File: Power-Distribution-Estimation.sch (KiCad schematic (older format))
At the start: 0 parts

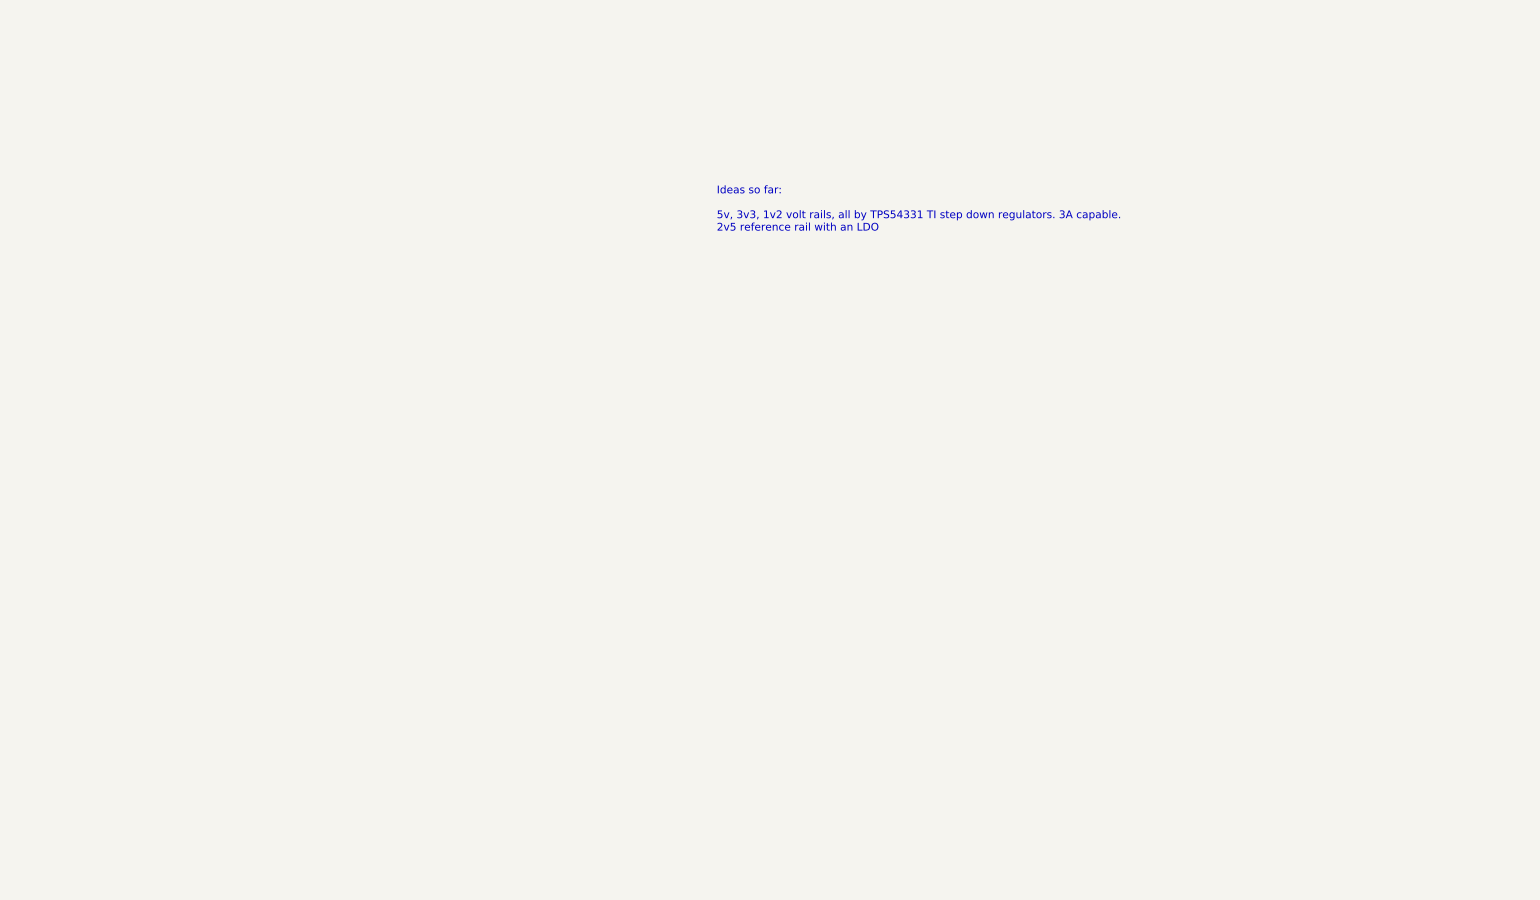
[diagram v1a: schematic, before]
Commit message: Continued work on schematic and board planning
Signed-off-by: Eldalote <Eldalote.Electronics@gmail.com>
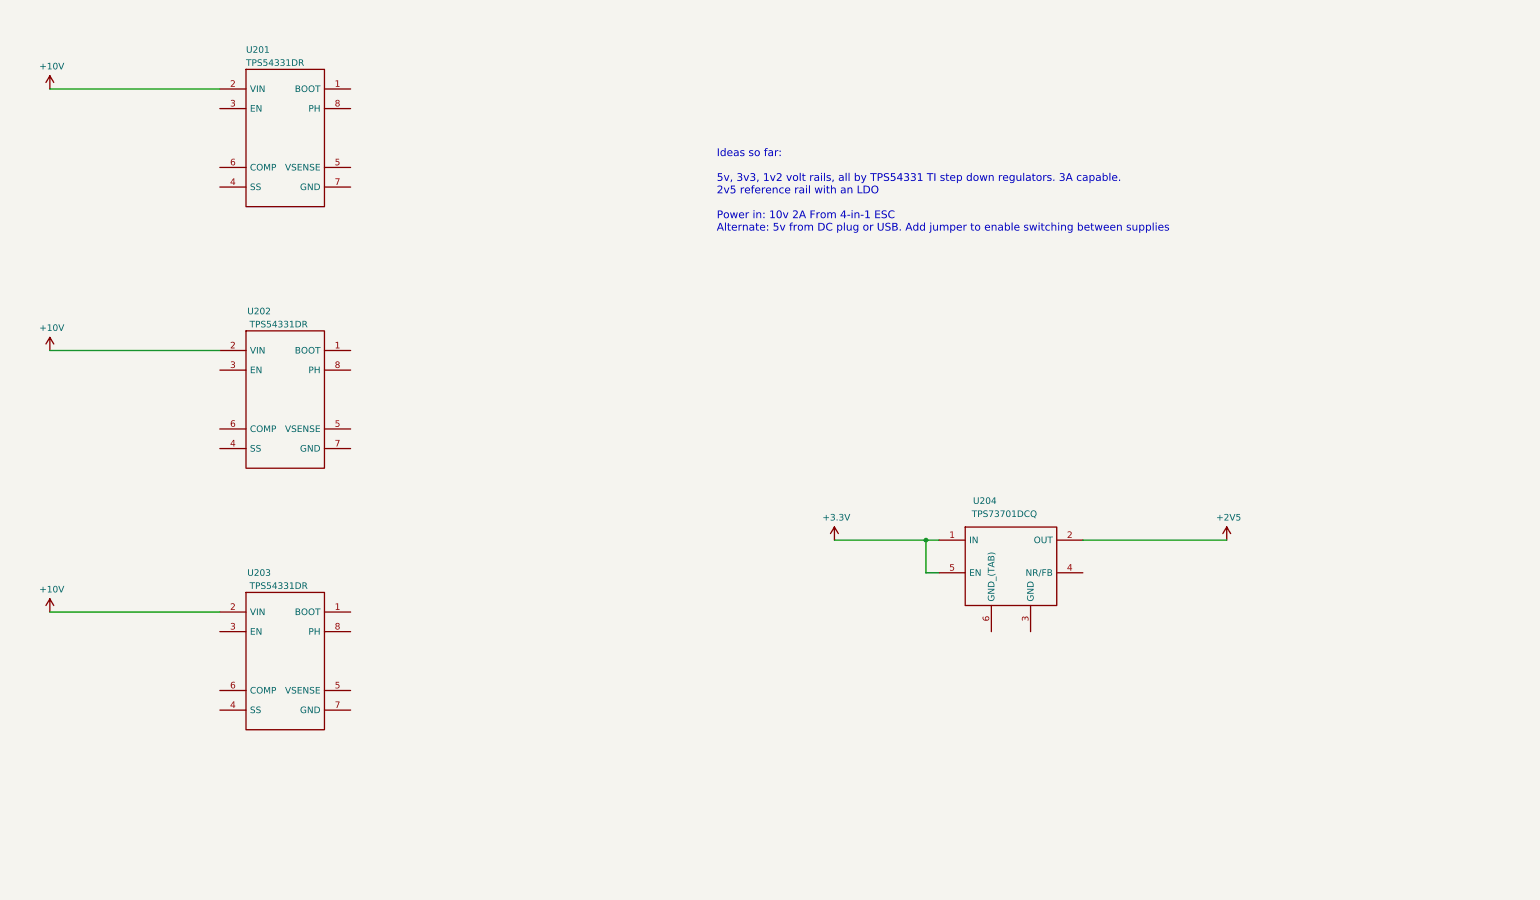
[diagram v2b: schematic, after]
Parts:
- added U201, U202, U203: TPS54331DR, SOIC127P600X175-8N, symbol SamacSys_Parts:TPS54331DR
- added U204: TPS73701DCQ, SOT127P706X180-6N, symbol SamacSys_Parts:TPS73701DCQ
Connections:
- new net +10V: U201.2 (VIN), U202.2 (VIN), U203.2 (VIN)
- new net +2V5: U204.2 (OUT)
- new net +3V3: U204.1 (IN), U204.5 (EN)
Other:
- note added: "Ideas so far:\n\n5v, 3v3, 1v2 volt rails, all by TPS54331 TI step down regulators. 3A capable.\n2v5 reference rail with an LDO\n\nPower in: 10v 2A From 4-in-1 ESC\nAlternate: 5v from DC plug or USB. Add jumper to enable switching between supplies"
- note removed: "Ideas so far:\n\n5v, 3v3, 1v2 volt rails, all by TPS54331 TI step down regulators. 3A capable.\n2v5 reference rail with an LDO"
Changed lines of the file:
@@
 $EndDescr
 Text Notes 6100 2250 0    59   ~ 0
-Ideas so far:\n\n5v, 3v3, 1v2 volt rails, all by TPS54331 TI step down regulators. 3A capable.\n2v5 reference rail with an LDO
+Ideas so far:\n\n5v, 3v3, 1v2 volt rails, all by TPS54331 TI step down regulators. 3A capable.\n2v5 reference rail with an LDO\n\nPower in: 10v 2A From 4-in-1 ESC\nAlternate: 5v from DC plug or USB. Add jumper to enable switching between supplies
+$Comp
+L SamacSys_Parts:TPS54331DR U201
+U 1 1 5F564651
+P 2300 1200
+F 0 "U201" H 2500 1550 50  0000 L CNN
+F 1 "TPS54331DR" H 2500 1450 50  0000 L CNN
+F 2 "SOIC127P600X175-8N" H 3350 1300 50  0001 L CNN
+F 3 "http://www.ti.com/lit/gpn/tps54331" H 3350 1200 50  0001 L CNN
+F 4 "Texas Instruments TPS54331DR, Step Down DC-DC Converter, 3A, Adjustable, 0.8  25 V, 8-Pin SOIC" H 3350 1100 50  0001 L CNN "Description"
+F 5 "1.75" H 3350 1000 50  0001 L CNN "Height"
+F 6 "595-TPS54331DR" H 3350 900 50  0001 L CNN "Mouser Part Number"
+F 7 "https://www.mouser.co.uk/ProductDetail/Texas-Instruments/TPS54331DR?qs=QyYHynRG50rsSYcB%2Ftz4Yw%3D%3D" H 3350 800 50  0001 L CNN "Mouser Price/Stock"
+F 8 "Texas Instruments" H 3350 700 50  0001 L CNN "Manufacturer_Name"
+F 9 "TPS54331DR" H 3350 600 50  0001 L CNN "Manufacturer_Part_Number"
+F 10 "595-TPS54331DR" H 2300 1200 50  0001 C CNN "Mouser"
+F 11 "296-26991-1-ND " H 2300 1200 50  0001 C CNN "DigiKey"
+F 12 "C9865" H 2300 1200 50  0001 C CNN "LCSC"
+	1    2300 1200
+	1    0    0    -1
+$EndComp
+$Comp
+L SamacSys_Parts:TPS54331DR U202
+U 1 1 5F5665A2
+P 2300 3200
+F 0 "U202" H 2600 3550 50  0000 C CNN
+F 1 "TPS54331DR" H 2750 3450 50  0000 C CNN
+F 2 "SOIC127P600X175-8N" H 3350 3300 50  0001 L CNN
+F 3 "http://www.ti.com/lit/gpn/tps54331" H 3350 3200 50  0001 L CNN
+F 4 "Texas Instruments TPS54331DR, Step Down DC-DC Converter, 3A, Adjustable, 0.8  25 V, 8-Pin SOIC" H 3350 3100 50  0001 L CNN "Description"
+F 5 "1.75" H 3350 3000 50  0001 L CNN "Height"
+F 6 "595-TPS54331DR" H 3350 2900 50  0001 L CNN "Mouser Part Number"
+F 7 "https://www.mouser.co.uk/ProductDetail/Texas-Instruments/TPS54331DR?qs=QyYHynRG50rsSYcB%2Ftz4Yw%3D%3D" H 3350 2800 50  0001 L CNN "Mouser Price/Stock"
+F 8 "Texas Instruments" H 3350 2700 50  0001 L CNN "Manufacturer_Name"
+F 9 "TPS54331DR" H 3350 2600 50  0001 L CNN "Manufacturer_Part_Number"
+F 10 "595-TPS54331DR" H 2300 3200 50  0001 C CNN "Mouser"
+F 11 "296-26991-1-ND " H 2300 3200 50  0001 C CNN "DigiKey"
+F 12 "C9865" H 2300 3200 50  0001 C CNN "LCSC"
+	1    2300 3200
+	1    0    0    -1
+$EndComp
+$Comp
+L SamacSys_Parts:TPS54331DR U203
+U 1 1 5F566CDB
+P 2300 5200
+F 0 "U203" H 2600 5550 50  0000 C CNN
+F 1 "TPS54331DR" H 2750 5450 50  0000 C CNN
+F 2 "SOIC127P600X175-8N" H 3350 5300 50  0001 L CNN
+F 3 "http://www.ti.com/lit/gpn/tps54331" H 3350 5200 50  0001 L CNN
+F 4 "Texas Instruments TPS54331DR, Step Down DC-DC Converter, 3A, Adjustable, 0.8  25 V, 8-Pin SOIC" H 3350 5100 50  0001 L CNN "Description"
+F 5 "1.75" H 3350 5000 50  0001 L CNN "Height"
+F 6 "595-TPS54331DR" H 3350 4900 50  0001 L CNN "Mouser Part Number"
+F 7 "https://www.mouser.co.uk/ProductDetail/Texas-Instruments/TPS54331DR?qs=QyYHynRG50rsSYcB%2Ftz4Yw%3D%3D" H 3350 4800 50  0001 L CNN "Mouser Price/Stock"
+F 8 "Texas Instruments" H 3350 4700 50  0001 L CNN "Manufacturer_Name"
+F 9 "TPS54331DR" H 3350 4600 50  0001 L CNN "Manufacturer_Part_Number"
+F 10 "595-TPS54331DR" H 2300 5200 50  0001 C CNN "Mouser"
+F 11 "296-26991-1-ND " H 2300 5200 50  0001 C CNN "DigiKey"
+F 12 "C9865" H 2300 5200 50  0001 C CNN "LCSC"
+	1    2300 5200
+	1    0    0    -1
+$EndComp
+$Comp
+L power:+10V #PWR0201
+U 1 1 5F56C393
+P 1000 1150
+F 0 "#PWR0201" H 1000 1000 50  0001 C CNN
+F 1 "+10V" H 1015 1323 50  0000 C CNN
+F 2 "" H 1000 1150 50  0001 C CNN
+F 3 "" H 1000 1150 50  0001 C CNN
+	1    1000 1150
+	1    0    0    -1
+$EndComp
+Wire Wire Line
+	1000 1150 2300 1150
+Wire Wire Line
+	2300 3150 1000 3150
+Wire Wire Line
+	2300 5150 1000 5150
+$Comp
+L power:+10V #PWR0202
+U 1 1 5F57758B
+P 1000 3150
+F 0 "#PWR0202" H 1000 3000 50  0001 C CNN
+F 1 "+10V" H 1015 3323 50  0000 C CNN
+F 2 "" H 1000 3150 50  0001 C CNN
+F 3 "" H 1000 3150 50  0001 C CNN
+	1    1000 3150
+	1    0    0    -1
+$EndComp
+$Comp
+L power:+10V #PWR0203
+U 1 1 5F577A69
+P 1000 5150
+F 0 "#PWR0203" H 1000 5000 50  0001 C CNN
+F 1 "+10V" H 1015 5323 50  0000 C CNN
+F 2 "" H 1000 5150 50  0001 C CNN
+F 3 "" H 1000 5150 50  0001 C CNN
+	1    1000 5150
+	1    0    0    -1
+$EndComp
+$Comp
+L SamacSys_Parts:TPS73701DCQ U204
+U 1 1 5F567988
+P 7800 4600
+F 0 "U204" H 8150 4900 50  0000 C CNN
+F 1 "TPS73701DCQ" H 8300 4800 50  0000 C CNN
+F 2 "SOT127P706X180-6N" H 9050 4700 50  0001 L CNN
+F 3 "http://www.ti.com/lit/ds/symlink/tps737.pdf" H 9050 4600 50  0001 L CNN
+F 4 "TPS73701DCQ, Low Dropout Voltage Regulator, Adjustable 1A, 1.2  5.5 V +/-1%, 6-Pin SOT-223" H 9050 4500 50  0001 L CNN "Description"
+F 5 "595-TPS73701DCQ " H 7800 4600 50  0001 C CNN "Mouser"
+F 6 "296-27066-1-ND" H 7800 4600 50  0001 C CNN "DigiKey"
+F 7 "-" H 7800 4600 50  0001 C CNN "LCSC"
+	1    7800 4600
+	1    0    0    -1
+$EndComp
+Wire Wire Line
+	7800 4600 7700 4600
+$Comp
+L power:+3.3V #PWR?
+U 1 1 5F585D3D
+P 7000 4600
+F 0 "#PWR?" H 7000 4450 50  0001 C CNN
+F 1 "+3.3V" H 7015 4773 50  0000 C CNN
+F 2 "" H 7000 4600 50  0001 C CNN
+F 3 "" H 7000 4600 50  0001 C CNN
+	1    7000 4600
+	1    0    0    -1
+$EndComp
+Wire Wire Line
+	8900 4600 10000 4600
+$Comp
+L power:+2V5 #PWR?
+U 1 1 5F58652C
+P 10000 4600
+F 0 "#PWR?" H 10000 4450 50  0001 C CNN
+F 1 "+2V5" H 10015 4773 50  0000 C CNN
+F 2 "" H 10000 4600 50  0001 C CNN
+F 3 "" H 10000 4600 50  0001 C CNN
+	1    10000 4600
+	1    0    0    -1
+$EndComp
+Wire Wire Line
+	7800 4850 7700 4850
+Wire Wire Line
+	7700 4850 7700 4600
+Connection ~ 7700 4600
+Wire Wire Line
+	7700 4600 7000 4600
 $EndSCHEMATC

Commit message: More of the same
Signed-off-by: Eldalote <Eldalote.Electronics@gmail.com>
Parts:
- added J201: PJ-102A, digikey-footprints:Barrel_Jack_5.5mmODx2.1mmID_PJ-102A, symbol dk_Barrel-Power-Connectors:PJ-102A
- added JP201: Jumper_NC_Dual, Connector_PinHeader_2.54mm:PinHeader_1x03_P2.54mm_Vertical, symbol Device:Jumper_NC_Dual
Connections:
- net labels added: +5V, 5v-plug, 5v-regulator, GND
- wire segments 8 -> 12
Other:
- note added: "Ideas so far:\n\n5v, 3v3, 1v2 volt rails, all by TPS54331 TI step down regulators. 3A capable.\n2v5 reference rail with an LDO\n1v8 for IMU \n\nPower in: 10v 2A From 4-in-1 ESC\nAlternate: 5v from DC plug or USB. Add jumper to enable switching between supplies"
- note removed: "Ideas so far:\n\n5v, 3v3, 1v2 volt rails, all by TPS54331 TI step down regulators. 3A capable.\n2v5 reference rail with an LDO\n\nPower in: 10v 2A From 4-in-1 ESC\nAlternate: 5v from DC plug or USB. Add jumper to enable switching between supplies"
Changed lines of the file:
@@
 $EndDescr
 Text Notes 6100 2250 0    59   ~ 0
-Ideas so far:\n\n5v, 3v3, 1v2 volt rails, all by TPS54331 TI step down regulators. 3A capable.\n2v5 reference rail with an LDO\n\nPower in: 10v 2A From 4-in-1 ESC\nAlternate: 5v from DC plug or USB. Add jumper to enable switching between supplies
+Ideas so far:\n\n5v, 3v3, 1v2 volt rails, all by TPS54331 TI step down regulators. 3A capable.\n2v5 reference rail with an LDO\n1v8 for IMU \n\nPower in: 10v 2A From 4-in-1 ESC\nAlternate: 5v from DC plug or USB. Add jumper to enable switching between supplies
 $Comp
 L SamacSys_Parts:TPS54331DR U201
@@
 	7800 4600 7700 4600
 $Comp
-L power:+3.3V #PWR?
+L power:+3.3V #PWR0101
 U 1 1 5F585D3D
 P 7000 4600
-F 0 "#PWR?" H 7000 4450 50  0001 C CNN
+F 0 "#PWR0101" H 7000 4450 50  0001 C CNN
 F 1 "+3.3V" H 7015 4773 50  0000 C CNN
 F 2 "" H 7000 4600 50  0001 C CNN
@@
 	8900 4600 10000 4600
 $Comp
-L power:+2V5 #PWR?
+L power:+2V5 #PWR0102
 U 1 1 5F58652C
 P 10000 4600
-F 0 "#PWR?" H 10000 4450 50  0001 C CNN
+F 0 "#PWR0102" H 10000 4450 50  0001 C CNN
 F 1 "+2V5" H 10015 4773 50  0000 C CNN
 F 2 "" H 10000 4600 50  0001 C CNN
@@
 Wire Wire Line
 	7700 4600 7000 4600
+$Comp
+L power:+5V #PWR0205
+U 1 1 5F5DB17B
+P 5850 6650
+F 0 "#PWR0205" H 5850 6500 50  0001 C CNN
+F 1 "+5V" H 5865 6823 50  0000 C CNN
+F 2 "" H 5850 6650 50  0001 C CNN
+F 3 "" H 5850 6650 50  0001 C CNN
+	1    5850 6650
+	1    0    0    -1
+$EndComp
+$Comp
+L Device:Jumper_NC_Dual JP201
+U 1 1 5F5DCDBD
+P 5850 6750
+F 0 "JP201" H 5850 6897 50  0000 C CNN
+F 1 "Jumper_NC_Dual" H 5850 6988 50  0000 C CNN
+F 2 "Connector_PinHeader_2.54mm:PinHeader_1x03_P2.54mm_Vertical" H 5850 6750 50  0001 C CNN
+F 3 "~" H 5850 6750 50  0001 C CNN
+F 4 "535-ME-100 " H 5850 6750 50  0001 C CNN "Mouser"
+F 5 "A860AR-ND" H 5850 6750 50  0001 C CNN "DigiKey"
+	1    5850 6750
+	-1   0    0    1
+$EndComp
+$Comp
+L dk_Barrel-Power-Connectors:PJ-102A J201
+U 1 1 5F5E0C37
+P 5100 6750
+F 0 "J201" H 5033 6975 50  0000 C CNN
+F 1 "PJ-102A" H 5033 6884 50  0000 C CNN
+F 2 "digikey-footprints:Barrel_Jack_5.5mmODx2.1mmID_PJ-102A" H 5300 6950 60  0001 L CNN
+F 3 "https://www.cui.com/product/resource/digikeypdf/pj-102a.pdf" H 5300 7050 60  0001 L CNN
+F 4 "490-PJ-102A" H 5100 6750 50  0001 C CNN "Mouser"
+F 5 "CP-102A-ND" H 5300 7150 60  0001 L CNN "DigiKey"
+	1    5100 6750
+	1    0    0    -1
+$EndComp
+$Comp
+L power:GND #PWR0204
+U 1 1 5F5E9A9C
+P 5400 7050
+F 0 "#PWR0204" H 5400 6800 50  0001 C CNN
+F 1 "GND" H 5405 6877 50  0000 C CNN
+F 2 "" H 5400 7050 50  0001 C CNN
+F 3 "" H 5400 7050 50  0001 C CNN
+	1    5400 7050
+	1    0    0    -1
+$EndComp
+Wire Wire Line
+	5600 6750 5200 6750
+Wire Wire Line
+	5400 7050 5400 6950
+Wire Wire Line
+	5400 6950 5200 6950
+Text Label 5250 6750 0    50   ~ 0
+5v-plug
+Wire Wire Line
+	6100 6750 6500 6750
+Text Label 6150 6750 0    50   ~ 0
+5v-regulator
 $EndSCHEMATC

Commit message: Further work
Signed-off-by: Eldalote <Eldalote.Electronics@gmail.com>
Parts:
- added C201: 22uF 25v, Capacitor_SMD:C_0805_2012Metric, symbol Device:C_Small
- added C202: 10pF, Capacitor_SMD:C_0402_1005Metric, symbol Device:C_Small
- added C203: 1nF, Capacitor_SMD:C_0402_1005Metric, symbol Device:C_Small
- added C204: 8n2F, Capacitor_SMD:C_0603_1608Metric, symbol Device:C_Small
- added C205: 100nF, Capacitor_SMD:C_0402_1005Metric, symbol Device:C_Small
- added C206, C207, C208: 47uF, Resistor_SMD:R_1206_3216Metric, symbol Device:C_Small
- added D201: 3A 60v, Diode_SMD:D_SMC, symbol Device:D_Schottky_Small
- added L201: 5u6H, Inductor_SMD:L_Bourns_SRN8040TA, symbol Device:L_Small
- added R201: 330K, Resistor_SMD:R_0402_1005Metric, symbol Device:R
- added R202: 68K, Resistor_SMD:R_0402_1005Metric, symbol Device:R
- added R203: 62K, Resistor_SMD:R_0603_1608Metric, symbol Device:R
- added R204: 10K, Resistor_SMD:R_0402_1005Metric, symbol Device:R
- added R205: 1.8K, Resistor_SMD:R_0603_1608Metric, symbol Device:R
- added R206: 100R, Resistor_SMD:R_0402_1005Metric, symbol Device:R
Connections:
- wire segments 12 -> 61
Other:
- moved on the sheet: U202, U203

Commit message: Made progress woth power
Signed-off-by: Jan Mart Liewes <Eldalote.Electronics@gmail.com>
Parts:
- removed C201: 22uF 25v, Capacitor_SMD:C_0805_2012Metric, symbol Device:C_Small
- removed C202: 10pF, Capacitor_SMD:C_0402_1005Metric, symbol Device:C_Small
- removed C203: 1nF, Capacitor_SMD:C_0402_1005Metric, symbol Device:C_Small
- removed C204: 8n2F, Capacitor_SMD:C_0603_1608Metric, symbol Device:C_Small
- removed C205: 100nF, Capacitor_SMD:C_0402_1005Metric, symbol Device:C_Small
- removed C206, C207, C208: 47uF, Resistor_SMD:R_1206_3216Metric, symbol Device:C_Small
- removed D201: 3A 60v, Diode_SMD:D_SMC, symbol Device:D_Schottky_Small
- removed L201: 5u6H, Inductor_SMD:L_Bourns_SRN8040TA, symbol Device:L_Small
- removed R201: 330K, Resistor_SMD:R_0402_1005Metric, symbol Device:R
- removed R202: 68K, Resistor_SMD:R_0402_1005Metric, symbol Device:R
- removed R203: 62K, Resistor_SMD:R_0603_1608Metric, symbol Device:R
- removed R204: 10K, Resistor_SMD:R_0402_1005Metric, symbol Device:R
- removed R205: 1.8K, Resistor_SMD:R_0603_1608Metric, symbol Device:R
- removed R206: 100R, Resistor_SMD:R_0402_1005Metric, symbol Device:R
- removed U201, U202, U203: TPS54331DR, SOIC127P600X175-8N, symbol SamacSys_Parts:TPS54331DR
- removed U204: TPS73701DCQ, SOT127P706X180-6N, symbol SamacSys_Parts:TPS73701DCQ
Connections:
- net labels removed: +10V, +2V5, +3.3V
- wire segments 61 -> 5
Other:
- note added: "5v DC plug and 5v rail jumper"
- note added: "Power requirements:\n1v2 (FPGA core): 1.5A estimated. Supply 2A to have margin. Derived from 5v rail. \n -- 1v2 at 2A is 2.4 watt. 90% regulator efficiency: 2.7 watt input. Around 540mA drain on 5v rail.\n -- Regulator: AP63200WU-7\n\n2v5 (FPGA PLL): 40mA estimated. Use small LDO, derived from 3v3. 40mA drain on 3v3 rail.\n -- Regulator: NCP115ASN250T2G\n\n3v3 (FPGA IO, sensors, radio, flash, LED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"
- note removed: "Ideas so far:\n\n5v, 3v3, 1v2 volt rails, all by TPS54331 TI step down regulators. 3A capable.\n2v5 reference rail with an LDO\n1v8 for IMU \n\nPower in: 10v 2A From 4-in-1 ESC\nAlternate: 5v from DC plug or USB. Add jumper to enable switching between supplies"
- moved on the sheet: J201, JP201
